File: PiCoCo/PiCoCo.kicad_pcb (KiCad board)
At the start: 2 copper layers, 98 x 65.2 mm, 54 parts, among them P1 COCO-CART, Q2 2N7002, Q3 2N7002, Q4 2N7002, U1 Pico 2 / RP2350B-Plus-W, U10 SN74LVC245A, U11 SN74LVC245A, U12 SN74LVC245A, U13 SN74LVC245A, U14 AMS1117-3.3, U15 SN74LVC00A

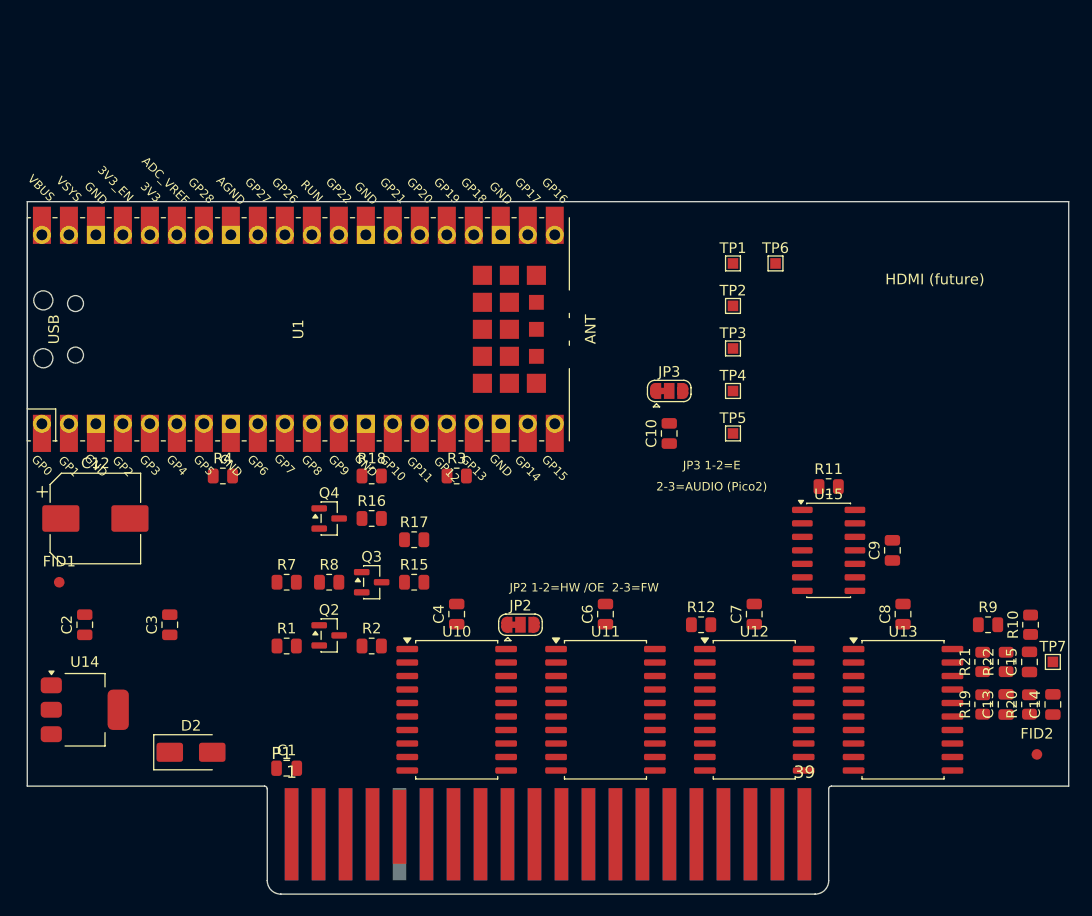
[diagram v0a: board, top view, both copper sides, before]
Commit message: kicad: v2.3 autoroute pass (Freerouting), 14 nets left for hand finish
Co-Authored-By: Claude Sonnet 5 <noreply@anthropic.com>
Claude-Session: https://claude.ai/code/session_013jbrP69zFzwzxjawTKy2c7
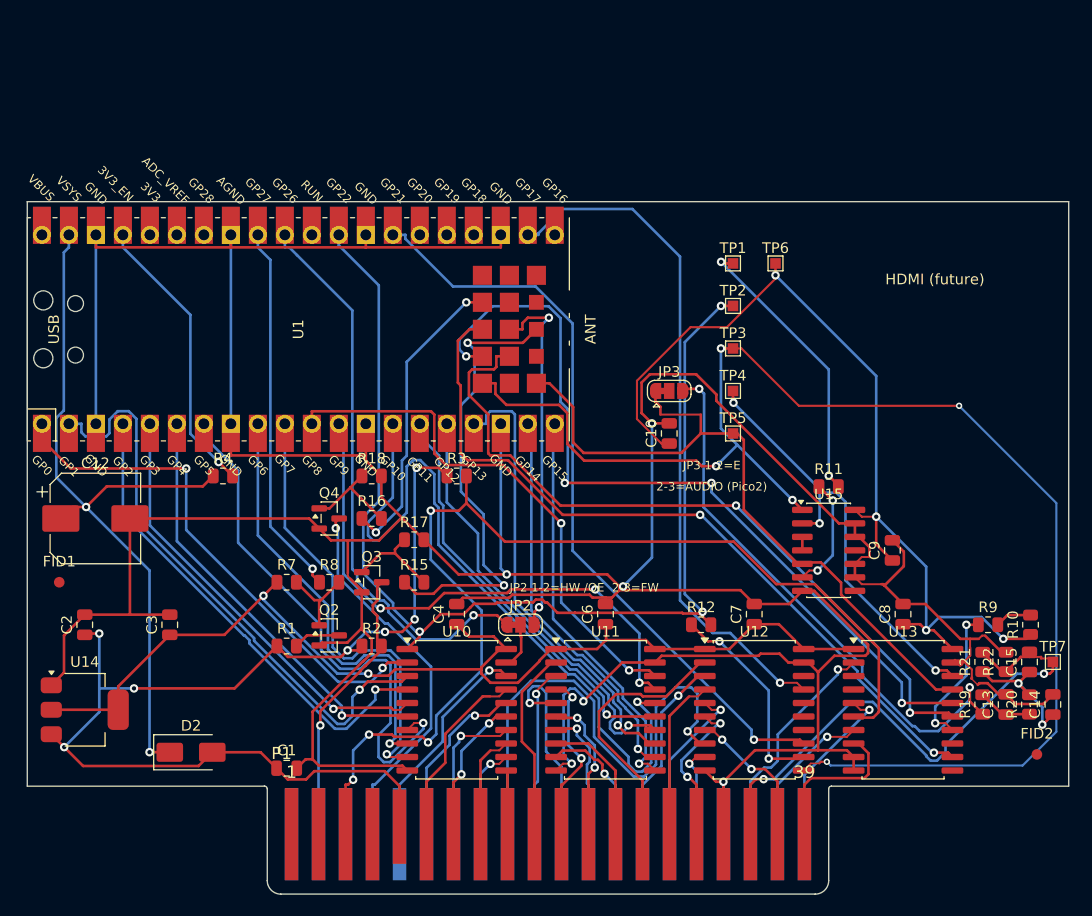
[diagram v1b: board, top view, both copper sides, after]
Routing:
- net GND: track 0.00 -> 448.2 mm, vias 0 -> 6
- net +3V3: track 0.00 -> 191.0 mm, vias 0 -> 6
- net CTS_BUF: track 0.00 -> 133.4 mm, vias 0 -> 5
- net +5V: track 0.00 -> 106.1 mm, vias 0 -> 7
- net RW_BUF: track 0.00 -> 106.0 mm, vias 0 -> 3
- net RESET_CART: track 0.00 -> 101.5 mm, vias 0 -> 4
- net OE_BUS: track 0.00 -> 80.6 mm, vias 0 -> 3
- net Q_BUF: track 0.00 -> 77.3 mm, vias 0 -> 4
- net A15_BUF: track 0.00 -> 71.9 mm, vias 0 -> 2
- net A13_BUF: track 0.00 -> 71.7 mm, vias 0 -> 1
- net VSYS_PICO: track 0.00 -> 70.7 mm, vias 0 -> 2
- net A2_BUF: track 0.00 -> 70.1 mm, vias 0 -> 1
- net SLENB_BUF: track 0.00 -> 69.1 mm, vias 0 -> 2
- net E_BUF: track 0.00 -> 67.2 mm
- net A9_BUF: track 0.00 -> 64.7 mm, vias 0 -> 1
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
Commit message: kicad: v2.3 fully routed, GND pours, DRC clean
- Default netclass 0.20 mm track / 0.15 mm clearance (was 0.25/0.20): lets
  Freerouting close 16 -> 7 nets; vias stay 0.8/0.4 mm.
- place_pcb: track/via keepouts round U1's four NPTH holes (hole clearance is
  not expressible in a Specctra DSN).
- tools/grid_route.py: A* grid router on pcbnew shape collisions; finished
  the 7 nets Freerouting could not (rip-up of U11's address stubs and the
  A6_BUF tail so U11 pin 10 GND could escape).
- tools/pour.py: GND pours both layers; tools/gnd_fix.py: links stray GND
  clusters (pads, vias, tracks, pour islands) and starved thermals.
- DRC (--severity-all --schematic-parity): 0 errors, 0 unconnected, 0 parity;
  77 silkscreen warnings remain (JLC clips silk over pads).

Co-Authored-By: Claude Fable 5.1 <noreply@anthropic.com>
Claude-Session: https://claude.ai/code/session_013jbrP69zFzwzxjawTKy2c7
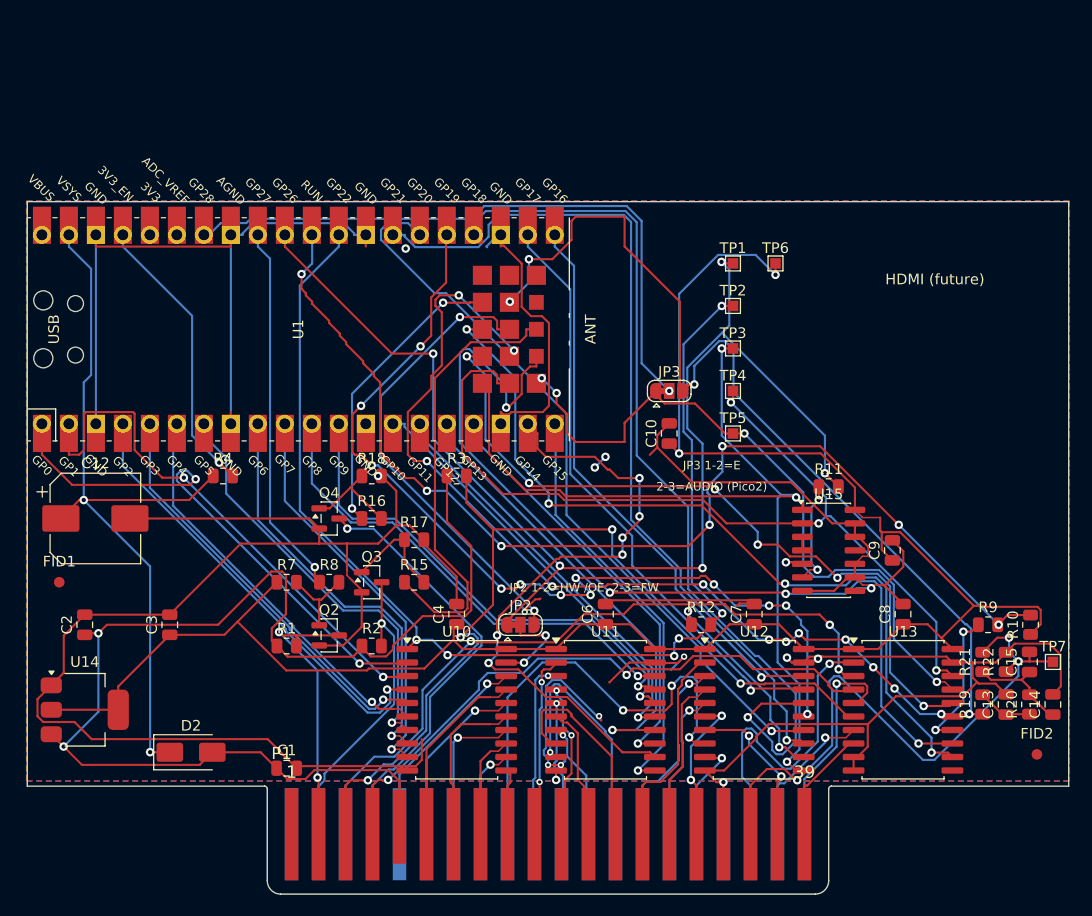
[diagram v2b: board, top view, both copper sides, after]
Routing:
- net PICO_RUN: track 3.47 -> 104.0 mm, vias 0 -> 7
- net A14_BUF: track 0.00 -> 88.5 mm, vias 0 -> 4
- net A11_BUF: track 0.00 -> 87.2 mm, vias 0 -> 12
- net A10_BUF: track 0.00 -> 85.3 mm, vias 0 -> 1
- net A12_BUF: track 0.00 -> 70.4 mm, vias 0 -> 1
- net E_CART: track 0.00 -> 66.5 mm, vias 0 -> 3
- net PICO_P34: track 0.00 -> 60.1 mm, vias 0 -> 1
- net Q_CART: track 0.00 -> 58.2 mm, vias 0 -> 2
- net A8_BUF: track 0.00 -> 53.7 mm, vias 0 -> 1
- net CTS_BUF: track 133.4 -> 86.1 mm, vias 5 -> 3
- net SCS_BUF: track 41.4 -> 86.2 mm
- net OE_BUS: track 80.6 -> 116.7 mm, vias 3 -> 5
- net AUDIO_PWM: track 52.7 -> 88.3 mm, vias 2 -> 4
- net A2_BUF: track 70.1 -> 38.3 mm
- net GND: track 448.2 -> 416.7 mm, vias 6 -> 14
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- added copper zone on B.Cu, net GND
- added copper zone on F.Cu, net GND

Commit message: kicad: review fixes for the routing tools and design rules
- grid_route.py: --pair only (no stale HINTS table), refills zones before
  saving, exit 1 on failure, documents the grid_route -> pour -> gnd_fix order.
- gnd_fix.py: exit 1 when a cluster stays open, empty-candidate guard, hint
  when --drc is omitted.
- pour.py: pour outline = board outline inset 0.3 mm, cut 1 mm above the
  finger area read from P1's rule areas (was a hardcoded 99.7); edit the
  zone's own outline (SetOutline hands over ownership and segfaults).
- Design rules: min track 0.127, min clearance 0.127, copper-to-edge 0.2
  (JLC floor). Re-poured; a redundant stitch via under U11 pin 10 removed.
- DRC --severity-all --schematic-parity: 0 errors, 0 unconnected, 0 parity,
  77 silk warnings.

Co-Authored-By: Claude Fable 5.1 <noreply@anthropic.com>
Claude-Session: https://claude.ai/code/session_013jbrP69zFzwzxjawTKy2c7
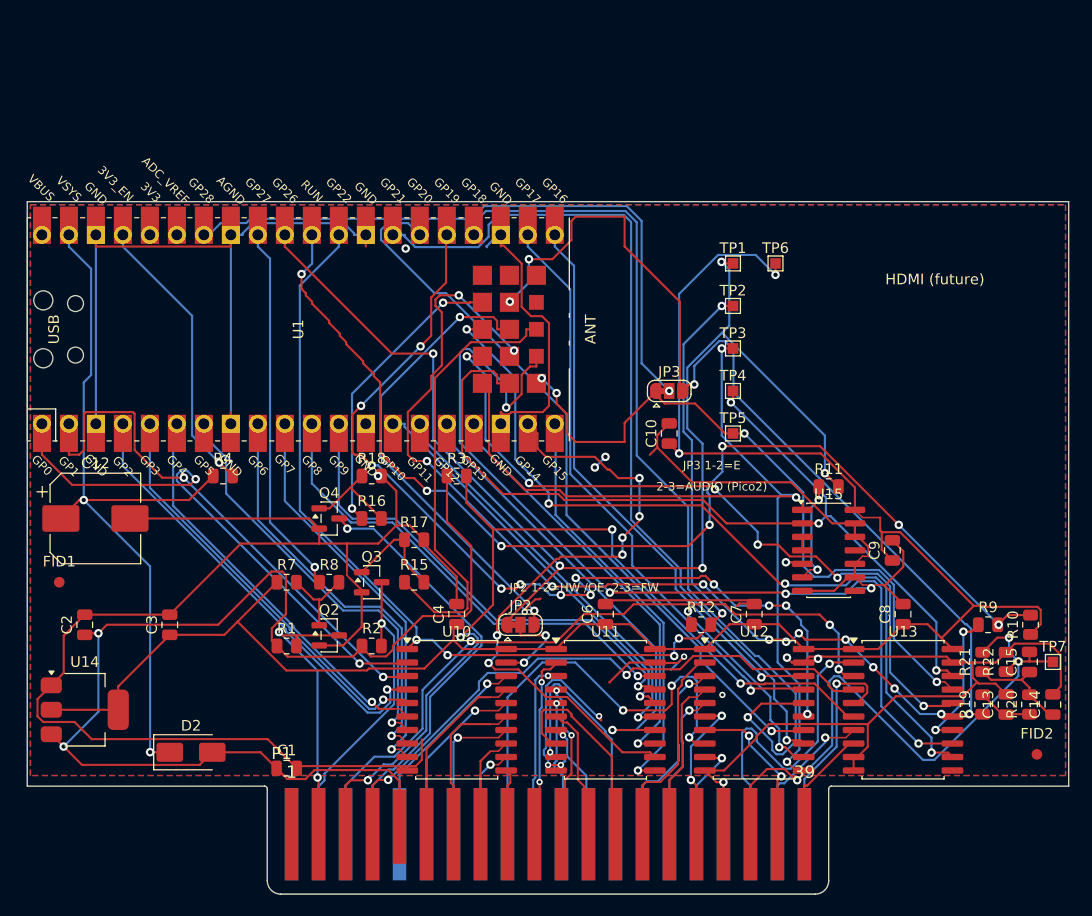
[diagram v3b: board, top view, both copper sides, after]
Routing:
- net GND: track 416.7 -> 415.9 mm
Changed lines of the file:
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@@
 	)
 	(segment
+		(start 165 90.6)
+		(end 165.017906 90.5951)
+		(width 0.2)
+		(layer "F.Cu")
+		(net "GND")
+	)
+	(segment
 		(start 147.893946 81.52585)
 		(end 147.8 81.6)
@@
 	)
 	(segment
-		(start 149.35 97.72)
-		(end 149.35 98.6)
-		(width 0.2)
-		(layer "F.Cu")
-		(net "GND")
-	)
-	(segment
 		(start 177.475 75.73)
 		(end 177.475 74.46)
@@
 	)
 	(via
-		(at 179.0147 80.5654)
-		(size 0.8)
-		(drill 0.4)
+		(at 165 90.6)
+		(size 0.6)
+		(drill 0.3)
 		(layers "F.Cu" "B.Cu")
 		(net "GND")
 	)
 	(via
-		(at 165.1 98.8139)
+		(at 179.0147 80.5654)
 		(size 0.8)
 		(drill 0.4)
@@
 	)
 	(via
-		(at 171.0807 87.0954)
+		(at 165.1 98.8139)
 		(size 0.8)
 		(drill 0.4)
@@
 	)
 	(via
-		(at 153 69.2)
+		(at 171.0807 87.0954)
 		(size 0.8)
 		(drill 0.4)
@@
 	)
 	(via
-		(at 149.35 98.6)
+		(at 153 69.2)
 		(size 0.8)
 		(drill 0.4)
@@
 	)
 	(segment
+		(start 164.9158 90.597231)
+		(end 165 90.6)
+		(width 0.2)
+		(layer "B.Cu")
+		(net "GND")
+	)
+	(segment
 		(start 149.8 89.2)
 		(end 153.2 92.6)
@@
 	)
 	(zone
+		(net "GND")
+		(layer "F.Cu")
+		(name "GND_F")
+		(hatch edge 0.5)
+		(connect_pads
+			(clearance 0.25)
+		)
+		(min_thickness 0.25)
+		(fill yes
+			(thermal_gap 0.3)
+			(thermal_bridge_width 0.4)
+			(island_removal_mode 0)
+		)
+		(polygon
+			(pts
+				(xy 197.29 98.187) (xy 99.89 98.187) (xy 99.89 44.487) (xy 197.29 44.487)
+			)
+		)
+	)
+	(zone
 		(layer "F.Cu")
 		(name "hdmi_reserved")
@@
 	)
 	(zone
-		(net "GND")
-		(layer "F.Cu")
-		(name "GND_F")
-		(hatch edge 0.5)
-		(connect_pads
-			(clearance 0.25)
-		)
-		(min_thickness 0.25)
-		(fill yes
-			(thermal_gap 0.3)
-			(thermal_bridge_width 0.4)
-			(island_removal_mode 0)
-		)
-		(polygon
-			(pts
-				(xy 99.5265 44.1235) (xy 197.6535 44.1235) (xy 197.6535 98.7) (xy 99.5265 98.7)
-			)
-		)
-	)
-	(zone
 		(layers "F.Cu" "B.Cu")
 		(name "antenna_keepout")
@@
 		(polygon
 			(pts
-				(xy 99.5265 44.1235) (xy 197.6535 44.1235) (xy 197.6535 98.7) (xy 99.5265 98.7)
+				(xy 197.29 98.187) (xy 99.89 98.187) (xy 99.89 44.487) (xy 197.29 44.487)
 			)
 		)

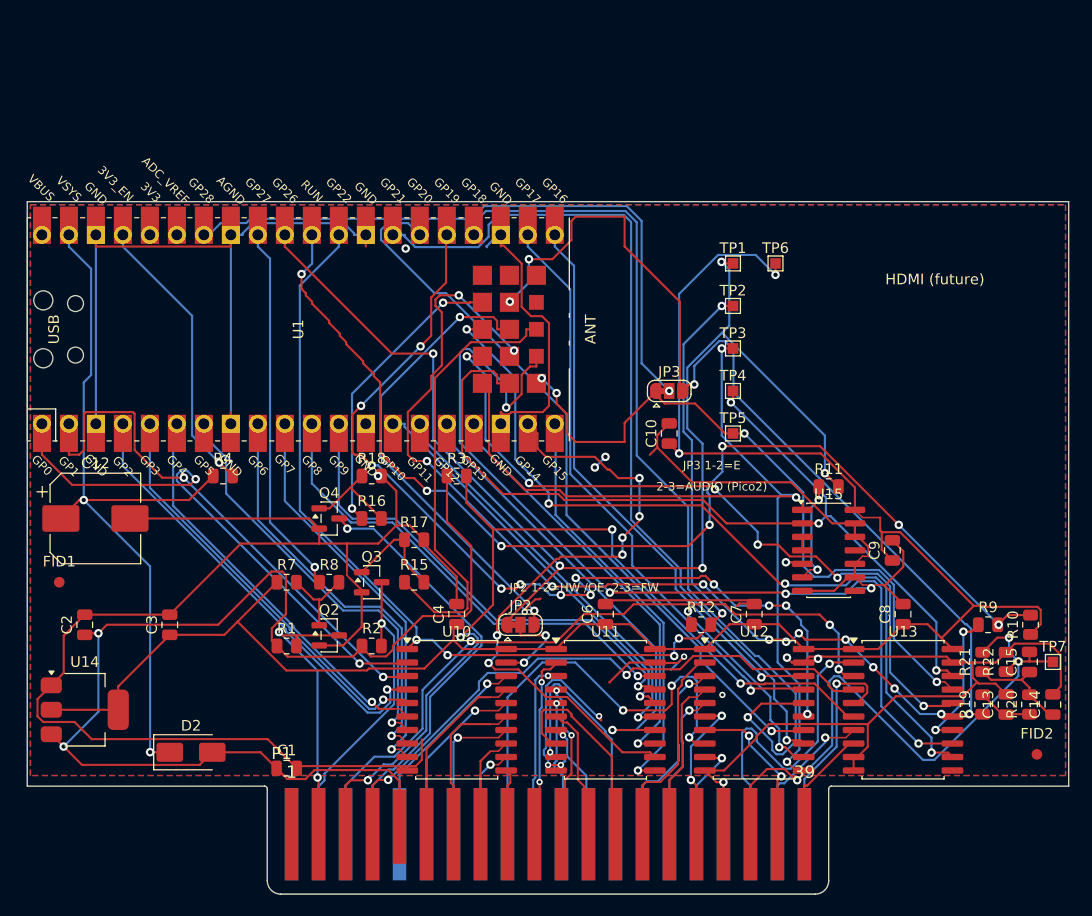
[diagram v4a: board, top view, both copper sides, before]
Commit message: kicad: v2.3.1 routed on the grown outline, DRC clean, fab package regenerated
Freerouting (100 passes, 0.20/0.15 netclass) + tools/finish_route.py (new
driver: strip GND, grid-route the leftovers, restore GND, pour, close GND,
DRC). grid_route via placement now honours hole-to-hole spacing across
nets. Cart GND/+5V neck tracks widened to 0.5 mm.

DRC --severity-all --schematic-parity: 0 errors, 0 unconnected, 0 parity,
61 silk warnings. BOM 16 lines, CPL 34 parts, module stencil 55 apertures,
production paste 177.

Co-Authored-By: Claude Fable 5.1 <noreply@anthropic.com>
Claude-Session: https://claude.ai/code/session_013jbrP69zFzwzxjawTKy2c7
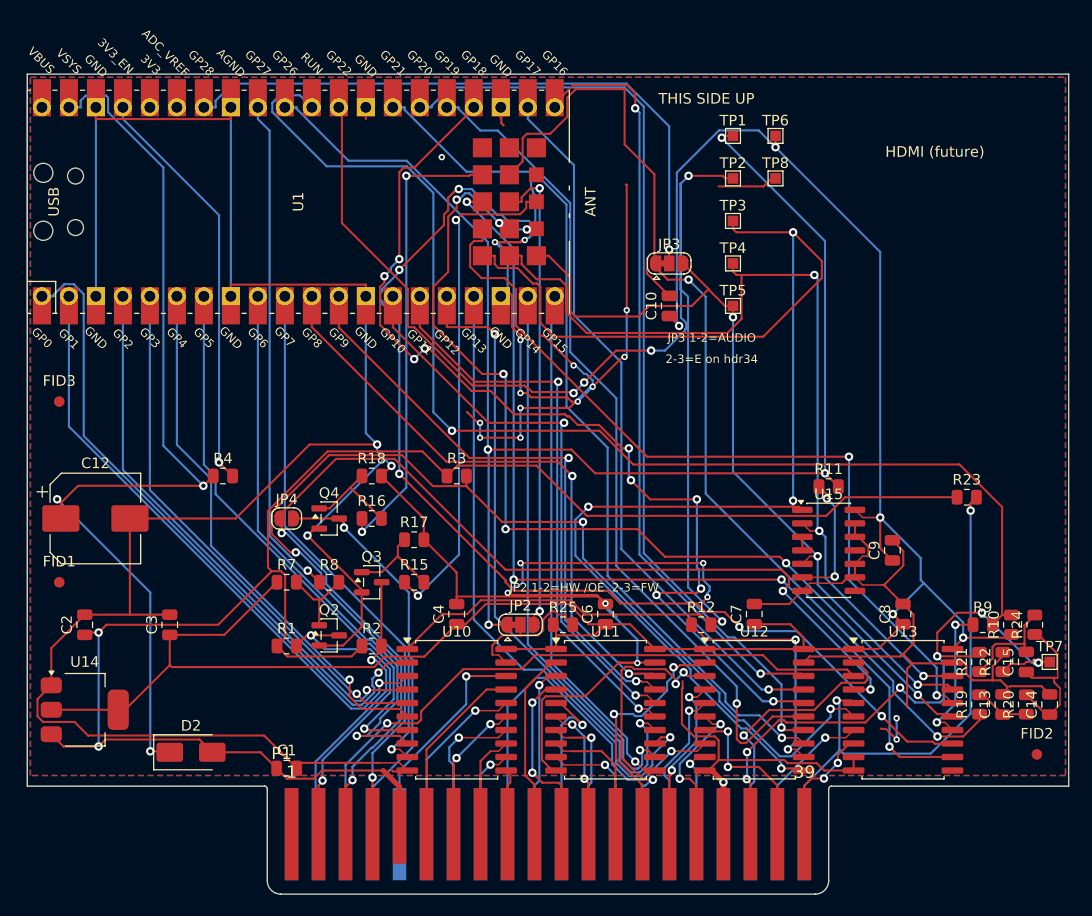
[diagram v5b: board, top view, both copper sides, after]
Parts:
- added FID3: FID, Fiducial:Fiducial_1mm_Mask2mm, F.Cu at (102.6, 63.0)
- added JP4: CART_TIE, Jumper:SolderJumper-2_P1.3mm_Open_RoundedPad1.0x1.5mm, F.Cu at (124.0, 74.0)
- added R23: 10k, Resistor_SMD:R_0805_2012Metric, F.Cu at (188.0, 72.0)
- added R24: 0, Resistor_SMD:R_0805_2012Metric, F.Cu at (194.4, 84.0)
- added R25: 10k, Resistor_SMD:R_0805_2012Metric, F.Cu at (150.0, 84.0)
- added TP8: GND, TestPoint:TestPoint_Pad_1.0x1.0mm, F.Cu at (170.0, 42.0)
- C15: value 100nF -> 1uF
- R7: value 100k -> 10k
- moved C10 12.0 mm to (160.0, 54.0)
- moved JP3 12.0 mm to (160.0, 50.0)
- moved TP1 12.0 mm to (166.0, 38.0)
- moved TP2 12.0 mm to (166.0, 42.0)
- moved TP3 12.0 mm to (166.0, 46.0)
- moved TP4 12.0 mm to (166.0, 50.0)
- moved TP5 12.0 mm to (166.0, 54.0)
- moved TP6 12.0 mm to (170.0, 38.0)
- moved U1 12.0 mm to (125.1, 44.2)
- moved R10 1.80 mm to (192.2, 84.0)
- moved R9 0.50 mm to (189.5, 84.0)
- moved C15 0.30 mm to (193.6, 87.5)
- moved R19 0.30 mm to (189.2, 91.5)
- moved R20 0.30 mm to (193.6, 91.5)
- moved R21 0.30 mm to (189.2, 87.5)
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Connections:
- C15 pad 2: SND_CART -> AUDIO_AC
- JP3 pad 1: E_BUF -> AUDIO_PWM
- JP3 pad 3: AUDIO_PWM -> E_BUF
- R21 pad 1: AUDIO_F2 -> AUDIO_AC
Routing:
- net GND: track 415.9 -> 508.3 mm, vias 14 -> 26
- net Q_CART: track 58.2 -> 107.0 mm, vias 2 -> 4
- net +5V: track 116.7 -> 164.8 mm
- net CTS_BUF: track 86.1 -> 133.6 mm, vias 3 -> 4
- net RW_BUF: track 110.2 -> 149.3 mm, vias 6 -> 5
- net +3V3: track 186.5 -> 221.3 mm, vias 2 -> 5
- net SLENB_CART: track 20.7 -> 50.4 mm, vias 1 -> 2
- net RESET_CART: track 87.1 -> 112.9 mm
- net VSYS_PICO: track 70.3 -> 91.4 mm, vias 2 -> 3
- net A5_BUF: track 39.8 -> 59.9 mm
- net A8_BUF: track 53.7 -> 72.9 mm, vias 1 -> 2
- net A12_BUF: track 70.4 -> 89.0 mm
- net A4_BUF: track 44.0 -> 61.9 mm, vias 1 -> 2
- net OE_BUS: track 116.7 -> 133.3 mm, vias 5 -> 4
- net CART_DRV: track 28.0 -> 43.7 mm
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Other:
- board size 98 x 65.2 mm -> 98 x 77.2 mm
- board text added: "2-3=E on hdr34"
- board text added: "JP3 1-2=AUDIO"
- board text added: "OTHER SIDE UP"
- board text added: "THIS SIDE UP"
- board text removed: "2-3=AUDIO (Pico2)"
- board text removed: "JP3 1-2=E"

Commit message: v2.3.1: silk revision, exact dimensions, bare-board README, review nits
- Back silk reads v2.3.1; checklist/spec/docs say 98 x 77.2 mm overall
  (67.0 mm body + 10.16 mm tongue), matching Edge.Cuts.
- README.md: orientation, power-off insertion, module mounting and the
  Pico 2 tape note, JP2/JP3/JP4 defaults, DNP list, TP map, flashing incl.
  BOOTSEL + CoCo RESET, images, Multi-Pak note.
- gen_schematic: R25 comment corrected. Fab package regenerated (silk only).

Co-Authored-By: Claude Fable 5.1 <noreply@anthropic.com>
Claude-Session: https://claude.ai/code/session_013jbrP69zFzwzxjawTKy2c7
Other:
- board text added: "PiCoCo v2.3.1 CERN-OHL-S-2.0"
- board text removed: "PiCoCo v2.3 CERN-OHL-S-2.0"

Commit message: kicad: drop the JLCJLCJLCJLC order-number placeholder (ordering with Remove Mark)
Co-Authored-By: Claude Fable 5.1 <noreply@anthropic.com>
Claude-Session: https://claude.ai/code/session_013jbrP69zFzwzxjawTKy2c7
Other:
- board text removed: "JLCJLCJLCJLC"
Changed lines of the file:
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@@
     (effects (font (size 0.8 0.8) (thickness 0.12)) (justify mirror))
-  )
-  (gr_text "JLCJLCJLCJLC" (at 110.0 62.0 0) (layer "B.SilkS")
-    (effects (font (size 1.0 1.0) (thickness 0.15)) (justify mirror))
   )
   (gr_text "JP2 1-2=HW /OE  2-3=FW" (at 152.0 80.5 0) (layer "F.SilkS")
